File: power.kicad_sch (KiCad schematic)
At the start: 30 parts, among them J3 Molex_Nano-Fit_1x2_SMD_105430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, Q1 DMPH4029LFGQ, Q2 BSS138-7-F, Q3 BSS138-7-F, U1 TPS56C230

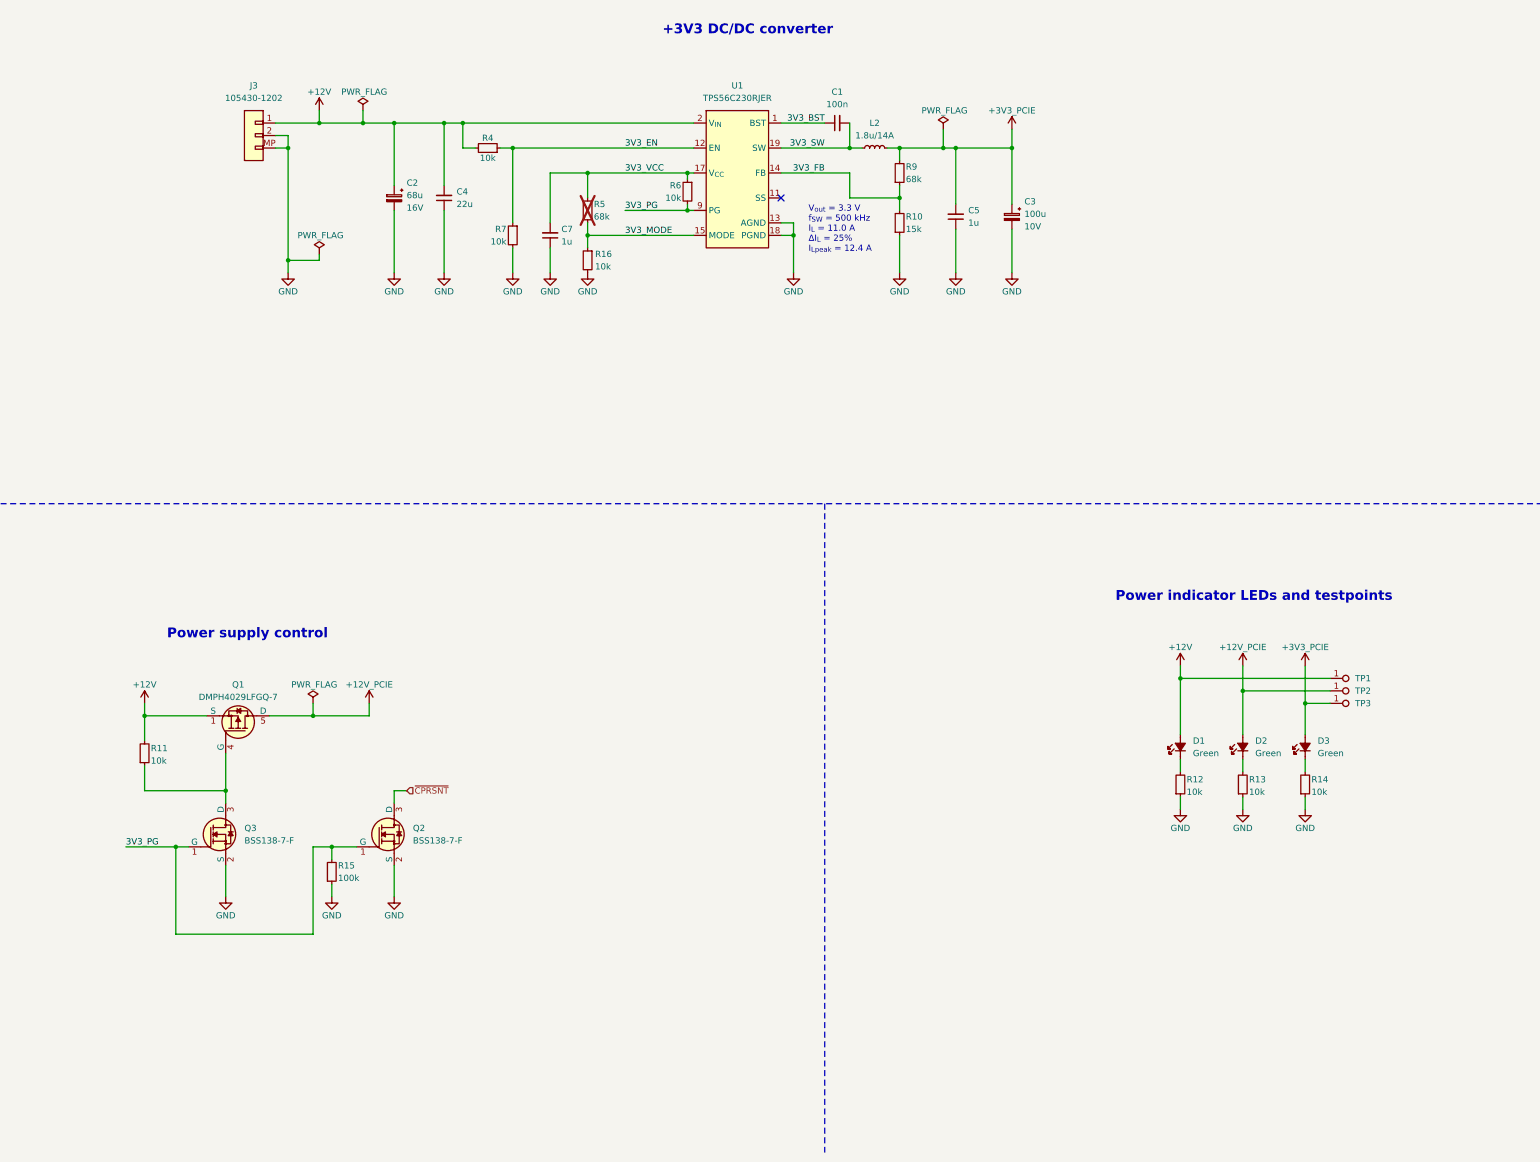
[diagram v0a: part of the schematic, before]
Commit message: [#79026] Change power input connector, add net classes, minor schematic refactor
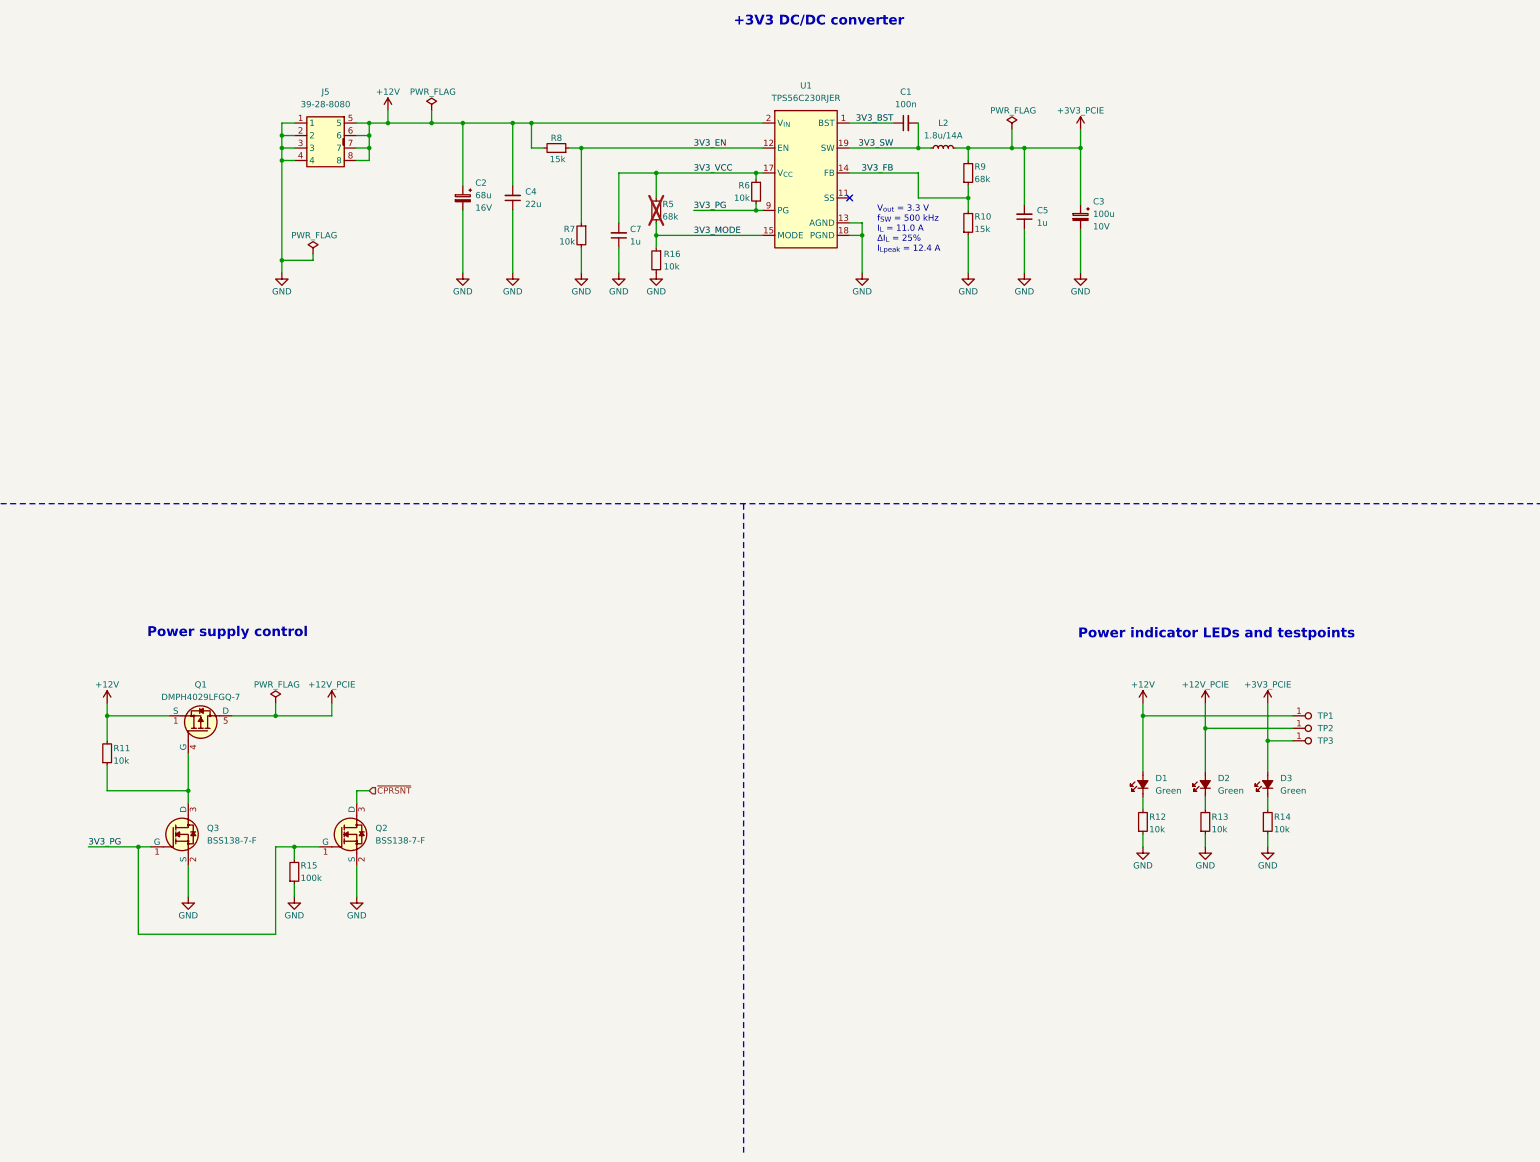
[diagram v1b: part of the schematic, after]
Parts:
- removed J3: Molex_Nano-Fit_1x2_SMD_1054301202, antmicro-footprints:Conn_Molex_Nano-Fit_1x2_SMD_1054301202, symbol antmicroWire2BoardConnectors:Molex_Nano-Fit_1x2_SMD_1054301202
- removed R4: R_10k_0402, antmicro-footprints:R_0402_1005Metric, symbol antmicroResistors0402:R_10k_0402
- added J5: Molex_Mini-Fit-Jr_2x4_39-28-8080, antmicro-footprints:MOLEX_39288080, symbol antmicroWire2BoardConnectors:Molex_Mini-Fit-Jr_2x4_39-28-8080
- added R8: R_15k_0402, antmicro-footprints:R_0402_1005Metric, symbol antmicroResistors0402:R_15k_0402
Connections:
- net +12V: now also J5.5, J5.6, J5.7, J5.8, R8.2
- net 3V3_EN: now also R8.1
- net GND: now also J5.1, J5.2, J5.3, J5.4
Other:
- moved on the sheet: C1, C2, C3, C4, C5, C7, D1, D2, D3, L2, Q1, Q2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

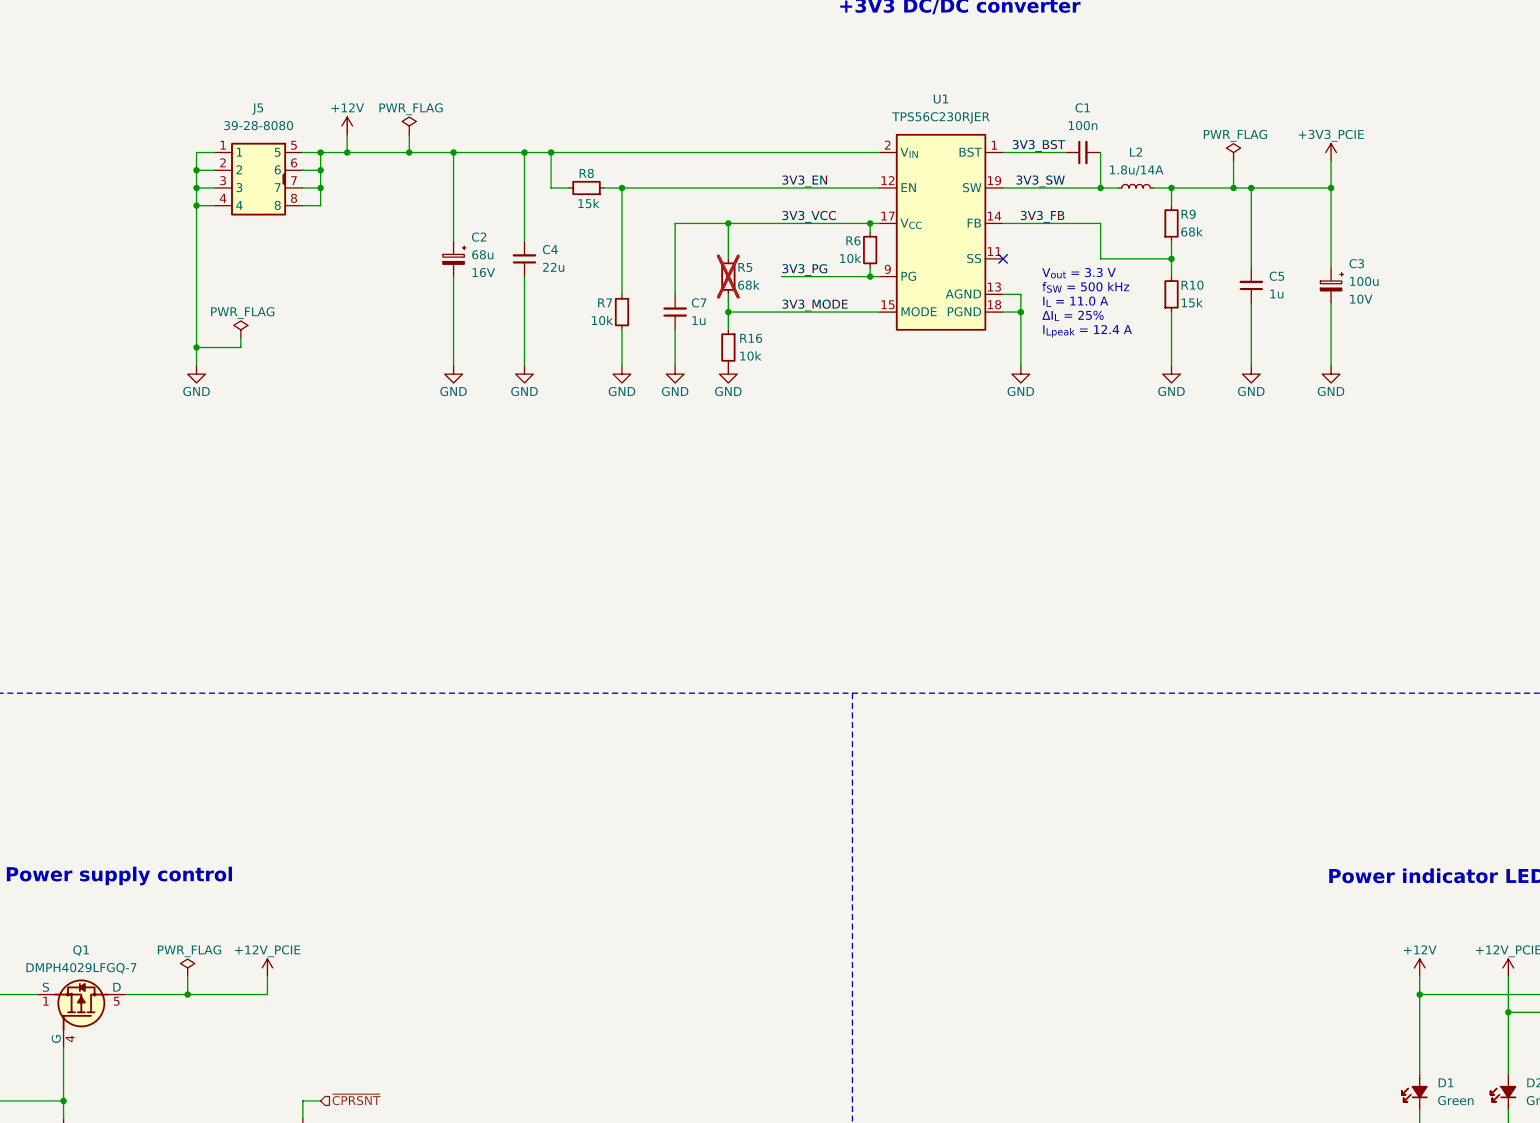
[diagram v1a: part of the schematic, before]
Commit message: [#79262] Begin component placement, add 12V PCIe decoupling capacitors, reduce inductor size
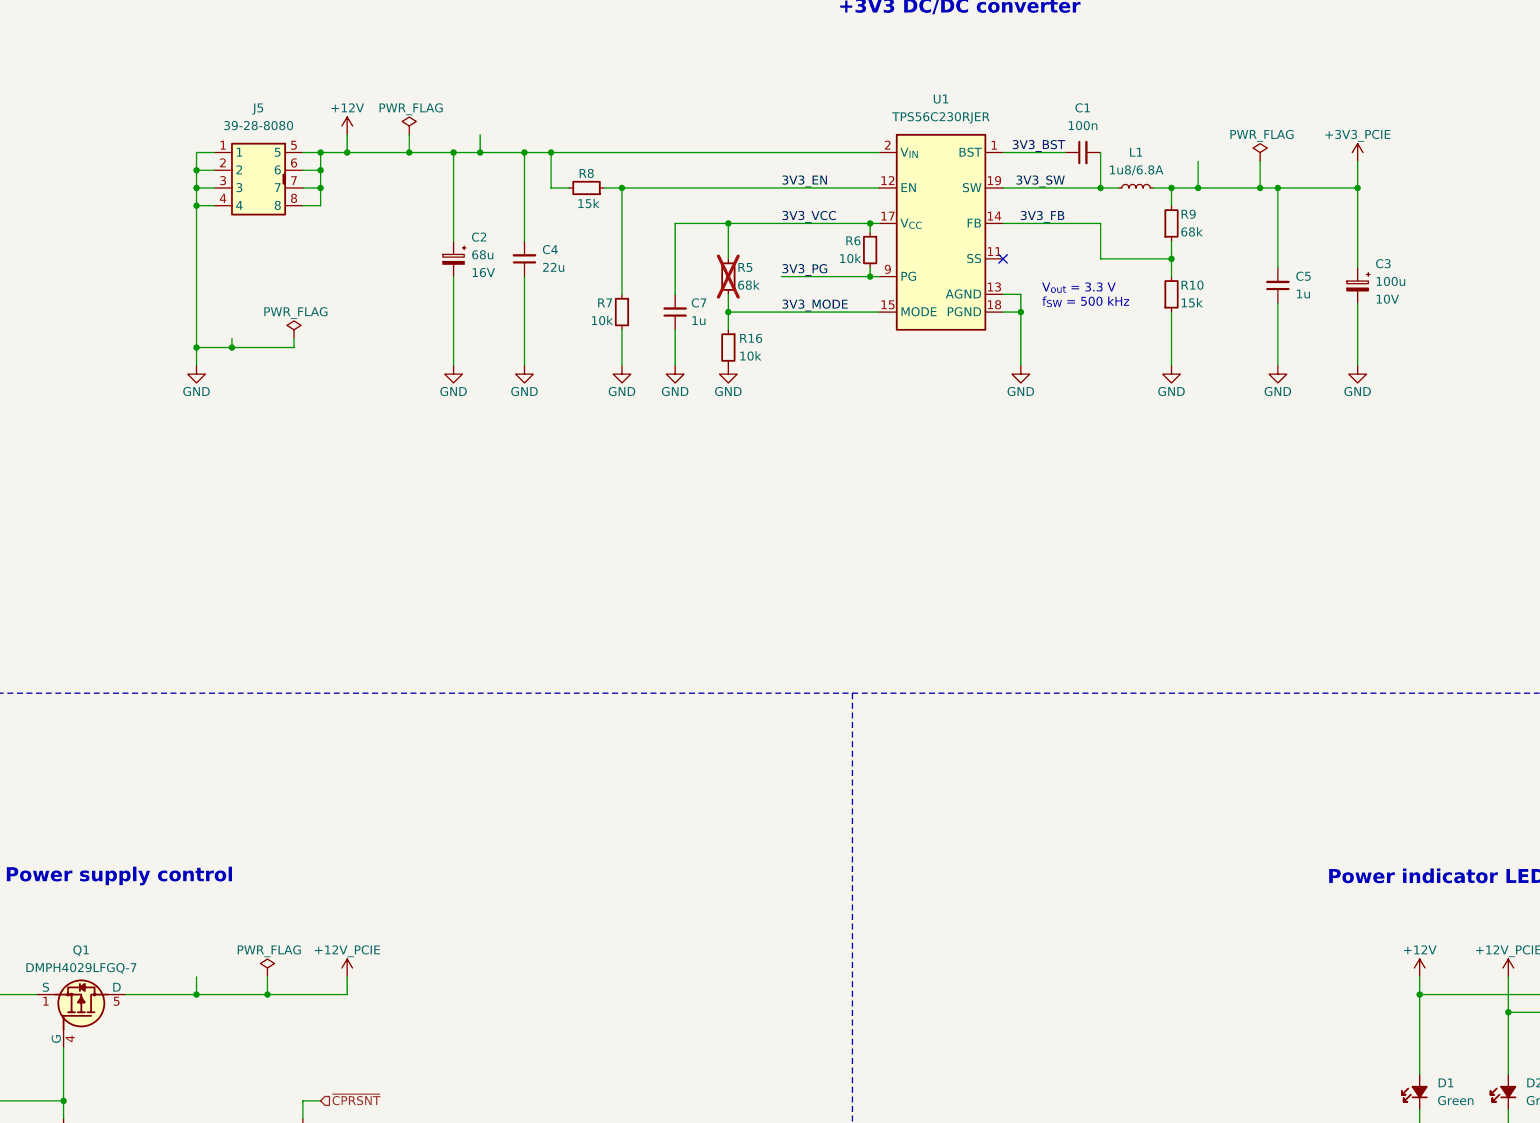
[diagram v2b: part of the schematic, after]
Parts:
- removed L2: L_1u8_14A_Coilcraft-XAL6030, antmicro-footprints:L_Coilcraft-XAL6030, symbol antmicroFixedInductors:L_1u8_14A_Coilcraft-XAL6030
- added L1: L_1u8_6.8A_WE-MAPI-4020, antmicro-footprints:L_WE-MAPI-4020, symbol antmicroFixedInductors:L_1u8_6.8A_WE-MAPI-4020
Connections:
- net +3V3_PCIE: now also L1.2
- net 3V3_SW: now also L1.1
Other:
- note added: "V_{out} = 3.3 V f_{SW} = 500 kHz"
- note removed: "V_{out} = 3.3 V f_{SW} = 500 kHz I_{L} = 11.0 A ΔI_{L} = 25% I_{Lpeak} = 12.4 A"
- moved on the sheet: C3, C5

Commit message: [#79262] Add USB PD input, 12V DC-DC converter, power ORing
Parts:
- added C16, C17: C_1u_25V_0603, antmicro-footprints:C_0603_1608Metric, symbol antmicroCapacitors0603:C_1u_25V_0603
- added C18, C19: C_100n_0402, antmicro-footprints:C_0402_1005Metric, symbol antmicroCapacitors0402:C_100n_0402
- added C20: C_1u_25V_0402, antmicro-footprints:C_0402_1005Metric, symbol antmicroCapacitors0402:C_1u_25V_0402
- added C21: C_4u7_25V_0402, antmicro-footprints:C_0402_1005Metric, symbol antmicroCapacitors0402:C_4u7_25V_0402
- added C22, C24, C25: C_10u_0805_35V, antmicro-footprints:C_0805_2012Metric, symbol antmicroCapacitorsmisc:C_10u_0805_35V
- added C23: C_33n_0402, antmicro-footprints:C_0402_1005Metric, symbol antmicroCapacitors0402:C_33n_0402
- added C26, C27, C31: C_100n_50V_X8L_0402, antmicro-footprints:C_0402_1005Metric, symbol antmicroCapacitors0402:C_100n_50V_X8L_0402
- added C28, C30: C_1n2_50V_0402, antmicro-footprints:C_0402_1005Metric, symbol antmicroCapacitors0402:C_1n2_50V_0402
- added C29: C_270p_25V_0402, antmicro-footprints:C_0402_1005Metric, symbol antmicroCapacitors0402:C_270p_25V_0402
- added C43, C44: C_Pol_150u_30V_Vishay-T59-EE, antmicro-footprints:C_Pol_Vishay-T59-EE, symbol antmicroCapacitorspol:C_Pol_150u_30V_Vishay-T59-EE
- added D5: AXGD10402KR, antmicro-footprints:D_0402_1005Metric, symbol antmicroTVSDiodes:AXGD10402KR
- added D8: LED_G_0603_LTST-C190GKT, antmicro-footprints:LED_0603_1608Metric_G, symbol antmicroLEDIndicationDiscrete:LED_G_0603_LTST-C190GKT
- added FB1, FB2: FB_10Z_10A_WE-MPSB_1206, antmicro-footprints:FB_1206_3216Metric, symbol antmicroFerriteBeadsandChips:FB_10Z_10A_WE-MPSB_1206
- added L2: L_4u7_14.6A_Abracon-Q8080, antmicro-footprints:L_Abracon_ASPIAIG-Q8080, symbol antmicroFixedInductors:L_4u7_14.6A_Abracon-Q8080
- added Q12, Q13: SI7613DN-T1-GE3, antmicro-footprints:Vishay_PowerPAK_1212-8_Single, symbol antmicroTransistorsFETsMOSFETsSingle:SI7613DN-T1-GE3
- added R23: R_2k_0402, antmicro-footprints:R_0402_1005Metric, symbol antmicroResistors0402:R_2k_0402
- added R29: R_10k_0402, antmicro-footprints:R_0402_1005Metric, symbol antmicroResistors0402:R_10k_0402
- added R30, R35: R_0R_0402, antmicro-footprints:R_0402_1005Metric, symbol antmicroResistors0402:R_0R_0402
- added R31: R_68k_0402, antmicro-footprints:R_0402_1005Metric, symbol antmicroResistors0402:R_68k_0402
- added R32, R34: R_100k_0402, antmicro-footprints:R_0402_1005Metric, symbol antmicroResistors0402:R_100k_0402
- added R33: R_158k_0402, antmicro-footprints:R_0402_1005Metric, symbol antmicroResistors0402:R_158k_0402
- added R36: R_3R3_0402, antmicro-footprints:R_0402_1005Metric, symbol antmicroResistors0402:R_3R3_0402
- added R37: R_8k66_0402, antmicro-footprints:R_0402_1005Metric, symbol antmicroResistors0402:R_8k66_0402
- added R38: R_316k_0402, antmicro-footprints:R_0402_1005Metric, symbol antmicroResistors0402:R_316k_0402
- added R39: R_10k_0.1%_0402, antmicro-footprints:R_0402_1005Metric, symbol antmicroResistors0402:R_10k_0.1%_0402
- added R40: R_140k_0.1%_0402, antmicro-footprints:R_0402_1005Metric, symbol antmicroResistors0402:R_140k_0.1%_0402
- added TP13: TP_0.75mm_SMD, antmicro-footprints:TP_SMD_0.75mm, symbol antmicroTestPoints:TP_0.75mm_SMD
- added U7, U8: LTC4412IS6, antmicro-footprints:SOT-23-6, symbol antmicroPMICORControllersIdealDiodes:LTC4412IS6
- added U9: SIC477ED-T1-GE3, antmicro-footprints:SIC47XED-T1-GE3, symbol antmicroDCDCConverters:SIC477ED-T1-GE3
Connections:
- net +12V: now also C30.2, C31.2, D5.2 (A), FB2.2, L2.2, R35.2, R40.2, TP13.1; no longer J5.5, J5.6, J5.7, J5.8
- net GND: now also C16.1, C17.1, C18.1, C19.1, C20.1, C21.1, C22.1, C23.2, C24.1, C25.1, C26.1, C29.2, C31.1, C43.2, C44.2, D5.1 (C), R23.2, R29.1, R31.1, R33.1, R39.1, U7.2 (GND), U7.3 (CTL), U8.2 (GND), U8.3 (CTL), U9.10 (PGND), U9.11 (PGND), U9.17 (PGND), U9.23 (AGND), U9.28 (AGND), U9.9 (PGND)
- new net: C22.2, C24.2, C25.2, C26.2, C43.1, C44.1, FB1.2, R32.2, U9.1 (V_{CIN}), U9.7 (V_{IN}), U9.8 (V_{IN})
- new net: R32.1, U9.3 (EN)
- new net: C16.2, C17.2, Q12.1 (S), Q12.2 (S), Q12.3 (S), Q13.1 (S), Q13.2 (S), Q13.3 (S), U7.6 (SENSE), U8.6 (SENSE)
- new net: R34.1, U9.2 (P_{GOOD})
- new net: C27.1, R36.1
- new net: R36.2, U9.5 (PHASE), U9.6 (PHASE)
- new net: R39.2, R40.1, U9.22 (V_{FB})
- new net: L2.1, R37.1, U9.12 (SW), U9.13 (SW), U9.14 (SW)
- new net: Q13.4 (G), U8.5 (GATE)
- new net: C18.2, J5.5, J5.6, J5.7, J5.8, Q13.5 (D), U8.1 (IN)
- new net: C27.2, U9.4 (BOOT)
- new net: D8.1 (C), R29.2
- new net: C28.1, R35.1, U9.20 (V_{SNS})
- new net: R38.1, U9.21 (NC)
- new net: C29.1, R38.2
- new net: Q12.4 (G), U7.5 (GATE)
- new net 12V_FSW: R33.2, U9.24 (f_{SW})
- new net 12V_ILIM: R30.2, R31.2, U9.25 (I_{LIMIT})
- new net 12V_MODE: R23.1, U9.27 (MODE)
- new net 12V_SNS: C28.2, C30.1, R37.2
- new net 12V_SS: C23.1, U9.19 (SS)
- new net VBUS: D8.2 (A)
- new net VCC: C19.2, FB1.1, FB2.1, Q12.5 (D), U7.1 (IN)
- new net VDD_12V_DCDC: C20.2, R30.1, R34.2, U9.26 (V_{DD})
- new net VDRV_12V_DCDC: C21.2, U9.16 (V_{DRV})
- no-connect marks 1 -> 5
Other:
- note added: "+12V DC/DC converter"
- note added: "0.8V typ"
- note added: "Assembly wariants: - 84W output (default) - 36W output (no SIC477 DC/DC converter, direct output from PD source) | Designator | 84W | 36W | | | | | | FB1 | populated | DNP | | FB2 | DNP | populated | | U2 | populated | DNP | | L1 | populated | DNP |"
- note added: "Note: Place close to the feedback resistors"
- note added: "Output current: max 7A"
- note added: "Pin used only in SIC472"
- note added: "Power ORing"
- note added: "Power save mode enabled, VDD, VDRVPre-reg on"
- note added: "R_FB_H = R_FB_L * (V_OUT - V_FB) / V_FB 10k * (12 - 0.8) / 0.8 = 140k"
- note added: "SIC477 can be substituted with SIC472. If so, some components need to be populated and some removed: | Designator | SIC477 | SIC472 | | | | | | R6 | populated | DNP | | R12 | populated | DNP | | R16 | DNP | populated | | R7 | DNP | populated | | R15 | DNP | populated | | C13 | DNP | populated | | C12 | DNP | populated | | C14 | DNP | populated |"
- note added: "USB PD power input"
- moved on the sheet: C1, C2, C3, C4, C5, C7, D1, D2, D3, J5, L1, Q1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
